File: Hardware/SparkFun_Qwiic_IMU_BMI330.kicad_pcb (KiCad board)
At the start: 2 copper layers, 25.4 x 25.4 mm, 54 parts, among them J1 Qwiic_RA, J2 Qwiic_RA, J3 Conn_01x06, J4 Conn_01x02, U1 BMI330

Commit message: Updated designs based on design review
- Nudged traces and vias
- Centered PTH
- Added Silkscreen for I2C/SPI
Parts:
- removed the G*** at (138.7, 87.3)
- removed kibuzzard-689A6711: G***, kibuzzard-689A6711
- removed kibuzzard-689A6718: G***, kibuzzard-689A6718
- removed kibuzzard-69FCDE2E: G***, kibuzzard-69FCDE2E
- removed kibuzzard-6A2C5E75: G***, kibuzzard-6A2C5E75
- removed kibuzzard-6A2C6D83 (x2): G***, kibuzzard-6A2C6D83
- removed kibuzzard-6A2C6EBA: G***, kibuzzard-6A2C6EBA
- removed kibuzzard-6A2C6EC4: G***, kibuzzard-6A2C6EC4
- removed kibuzzard-6A2C6EE6: G***, kibuzzard-6A2C6EE6
- removed kibuzzard-6A2C6EED: G***, kibuzzard-6A2C6EED
- added kibuzzard-6A2AF6B9: G***, kibuzzard-6A2AF6B9, B.Cu at (141.1, 100.7)
- added kibuzzard-6A2AF6DB: G***, kibuzzard-6A2AF6DB, B.Cu at (141.0, 102.6)
- added kibuzzard-6A34231C: G***, kibuzzard-6A34231C, B.Cu at (129.7, 100.3)
- added kibuzzard-6A343325: G***, kibuzzard-6A343325, B.Cu at (136.0, 98.5)
- added kibuzzard-6A39953E: G***, kibuzzard-6A39953E, F.Cu at (136.0, 93.0)
- added kibuzzard-6A3997C3: G***, kibuzzard-6A3997C3, B.Cu at (133.7, 100.3)
- added kibuzzard-6A3997C3: G***, kibuzzard-6A3997C3, B.Cu at (137.3, 102.7)
- added kibuzzard-6A3997C3: G***, kibuzzard-6A3997C3, B.Cu at (133.7, 102.7)
- added kibuzzard-6A3997C3: G***, kibuzzard-6A3997C3, B.Cu at (133.7, 105.0)
- added kibuzzard-6A399819: G***, kibuzzard-6A399819, B.Cu at (143.2, 104.3)
- added kibuzzard-6A39988E: G***, kibuzzard-6A39988E, B.Cu at (142.3, 107.3)
- added kibuzzard-6A399897: G***, kibuzzard-6A399897, F.Cu at (142.3, 107.3)
- added kibuzzard-6A399913: G***, kibuzzard-6A399913, F.Cu at (139.8, 107.0)
- added kibuzzard-6A399936: G***, kibuzzard-6A399936, B.Cu at (134.7, 107.0)
- added kibuzzard-6A39993E: G***, kibuzzard-6A39993E, B.Cu at (137.2, 107.2)
- added kibuzzard-6A39994B: G***, kibuzzard-6A39994B, B.Cu at (139.8, 107.0)
- added kibuzzard-6A399BFC: G***, kibuzzard-6A399BFC, B.Cu at (136.0, 101.6)
- added kibuzzard-6A399D08: G***, kibuzzard-6A399D08, B.Cu at (144.9, 91.3)
- added kibuzzard-6A399D19: G***, kibuzzard-6A399D19, B.Cu at (144.9, 92.4)
- added kibuzzard-6A399D1E: G***, kibuzzard-6A399D1E, B.Cu at (144.8, 93.5)
- G***: footprint SparkFun-Aesthetic:SparkFun_Logo_10mm -> SparkFun-Aesthetic:SparkFun_Logo_12.5mm
- moved J4 5.08 mm to (137.2, 86.7)
- moved kibuzzard-6A2C6F4B 5.08 mm to (137.2, 89.2) (x2)
- moved kibuzzard-6A2C6F56 5.08 mm to (134.7, 89.2) (x2)
- moved G*** 2.95 mm to (129.4, 91.7)
- moved G*** 2.74 mm to (136.0, 95.8)
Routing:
- net GND: track 11.3 -> 6.56 mm
- net 3.3V: track 50.5 -> 47.2 mm, vias 6 -> 5
- net INT1: track 13.6 -> 11.0 mm
- net INT2: track 14.0 -> 12.1 mm
- net SDA/PICO: track 44.0 -> 43.1 mm
- net POCI: track 12.5 -> 11.7 mm
- net Net-(JP1-A): track 3.04 -> 2.41 mm

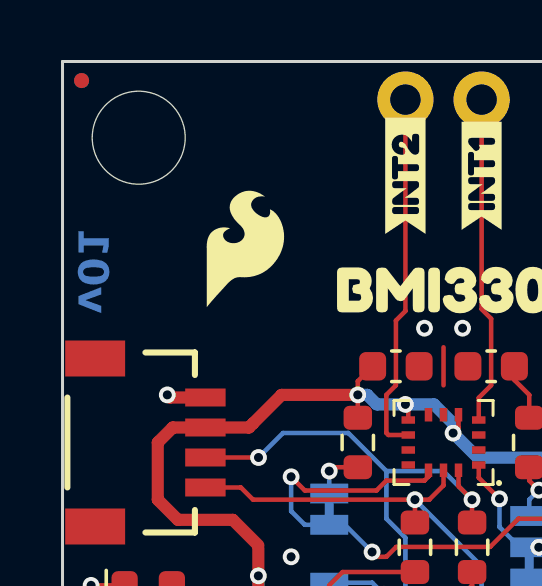
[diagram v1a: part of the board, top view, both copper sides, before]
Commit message: Changed IC PROD_ID and updated silk to v10
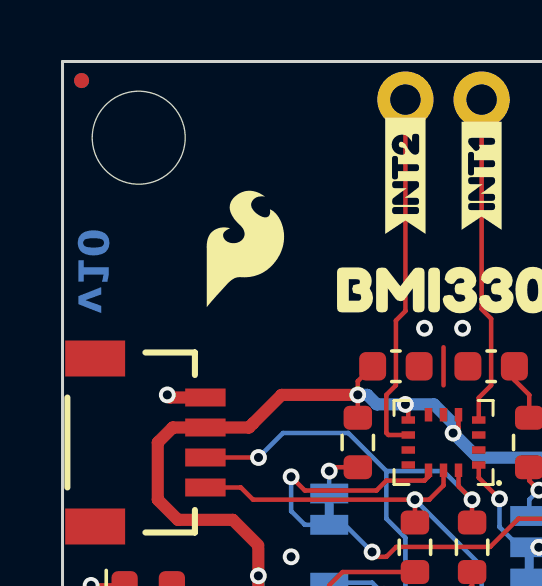
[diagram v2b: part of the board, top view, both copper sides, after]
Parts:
- JP3: value CSB -> ~{CS}
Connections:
- net CSB renamed ~{CS}
- net POCI renamed SDO/POCI
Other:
- board text added: "v10"
- board text removed: "v01"
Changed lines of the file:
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@@
 	(net 7 "unconnected-(J2-NC-PadNC2)")
 	(net 8 "Net-(JP1-A)")
-	(net 9 "POCI")
-	(net 10 "CSB")
+	(net 9 "SDO{slash}POCI")
+	(net 10 "~{CS}")
 	(net 11 "INT1")
 	(net 12 "INT2")
@@
 			(keep_end_layers yes)
 			(zone_layer_connections)
-			(net 9 "POCI")
+			(net 9 "SDO{slash}POCI")
 			(pinfunction "Pin_5")
 			(pintype "passive")
@@
 			(keep_end_layers yes)
 			(zone_layer_connections)
-			(net 10 "CSB")
+			(net 10 "~{CS}")
 			(pinfunction "Pin_6")
 			(pintype "passive")
@@
 			)
 		)
-		(property "PROD_ID" "IC-18009"
+		(property "PROD_ID" "IC-28800"
 			(at 0 0 180)
 			(unlocked yes)
@@
 			(size 0.45 0.25)
 			(layers "F.Cu" "F.Mask" "F.Paste")
-			(net 9 "POCI")
+			(net 9 "SDO{slash}POCI")
 			(pinfunction "SDO")
 			(pintype "bidirectional")
@@
 			(size 0.45 0.25)
 			(layers "F.Cu" "F.Mask" "F.Paste")
-			(net 10 "CSB")
+			(net 10 "~{CS}")
 			(pinfunction "~{CS}")
 			(pintype "bidirectional")
@@
 			(size 0.6604 1.27)
 			(layers "B.Cu" "B.Mask")
-			(net 9 "POCI")
+			(net 9 "SDO{slash}POCI")
 			(pinfunction "B")
 			(pintype "passive")
@@
 				(font
 					(size 0.001 0.001)
+					(thickness 0.15)
 				)
 				(justify mirror)
@@
 				(font
 					(size 0.001 0.001)
+					(thickness 0.15)
 				)
 				(justify mirror)
@@
 				(font
 					(size 0.001 0.001)
+					(thickness 0.15)
 				)
 				(justify mirror)
@@
 				(font
 					(size 0.001 0.001)
+					(thickness 0.15)
 				)
 				(justify mirror)
@@
 				(font
 					(size 0.001 0.001)
+					(thickness 0.15)
 				)
 				(justify mirror)
@@
 				(font
 					(size 0.001 0.001)
+					(thickness 0.15)
 				)
 				(justify mirror)
@@
 			)
 		)
-		(property "Value" "CSB"
+		(property "Value" "~{CS}"
 			(at 0 -1.143 90)
 			(layer "B.Fab")
@@
 			(size 0.6604 1.27)
 			(layers "B.Cu" "B.Mask")
-			(net 10 "CSB")
+			(net 10 "~{CS}")
 			(pinfunction "A")
 			(pintype "passive")
@@
 		(layer "Edge.Cuts")
 	)
-	(gr_text "v01"
+	(gr_text "v10"
 		(at 124.264 92.391 270)
 		(layer "B.Cu" knockout)
